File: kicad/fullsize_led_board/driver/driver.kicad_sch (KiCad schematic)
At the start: 131 parts, among them J4 Anodes Header, J5 Cathodes Header, Q1 SQ2351CES, Q10 SQ2351CES, Q11 SQ2351CES, Q12 SQ2351CES, Q13 SQ2351CES, Q14 SQ2351CES, Q15 SQ2351CES, Q16 SQ2351CES, Q17 SQ2351CES, Q18 SQ2351CES, Q19 SQ2351CES, Q2 SQ2351CES, Q20 SQ2351CES, Q21 SQ2351CES, Q22 SQ2351CES, Q23 SQ2351CES, Q24 SQ2351CES, Q3 SQ2351CES, Q4 SQ2351CES, Q5 SQ2351CES, Q6 SQ2351CES, Q7 SQ2351CES, Q8 SQ2351CES, Q9 SQ2351CES, U1 74HCT541, U2 74HCT595, U3 74HCT595, U4 74HCT595, U5 TPIC6B595N, U6 TPIC6B595N, U7 TPIC6B595N, U8 TPIC6B595N

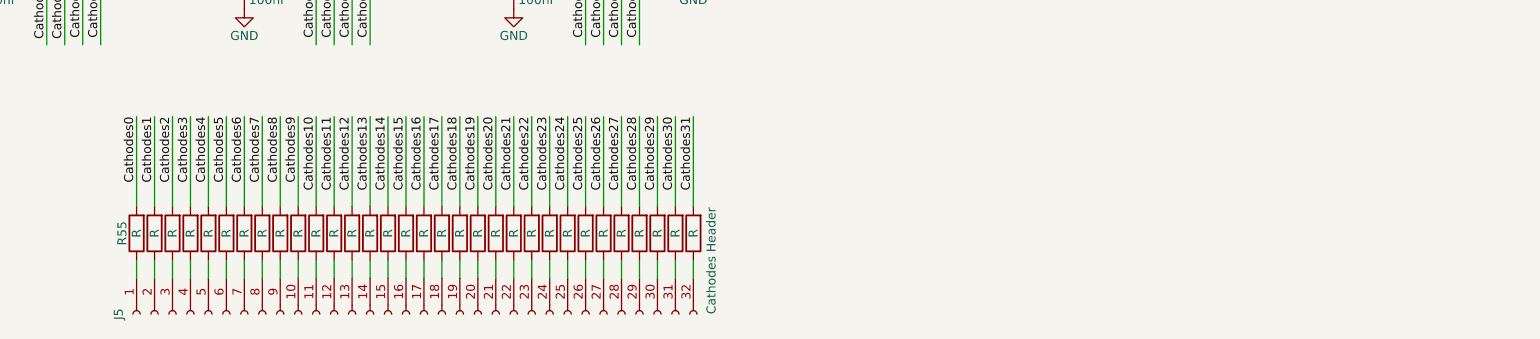
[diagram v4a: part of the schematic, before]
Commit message: kicad: finalized led resistor values
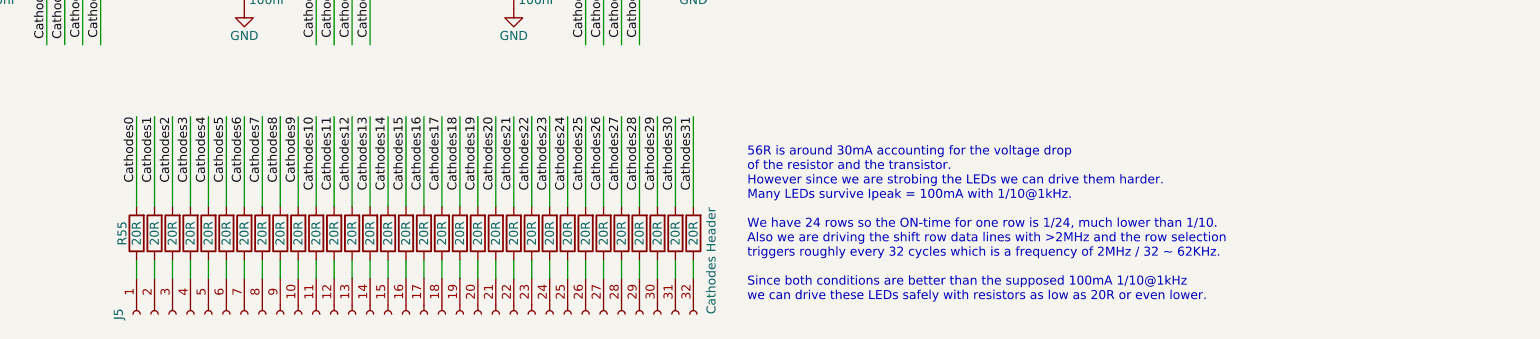
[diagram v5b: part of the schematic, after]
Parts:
- R55, R56, R57, R58, R59, R60, R61, R62, R63, R64, R65, R66, R67, R68, R69, R70, R71, R72, R73, R74, R75, R76, R77, R78, R79, R80, R81, R82, R83, R84, R85, R86: value R -> 20R
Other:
- note added: "56R is around 30mA accounting for the voltage drop of the resistor and the transistor. However since we are strobing the LEDs we can drive them harder. Many LEDs survive Ipeak = 100mA with 1/10@1kHz. We have 24 rows so the ON-time for one row is 1/24, much lower than 1/10. Also we are driving the shift row data lines with >2MHz and the row selection triggers roughly every 32 cycles which is a fre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"
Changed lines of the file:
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@@
 		)
 	)
+	(text "56R is around 30mA accounting for the voltage drop\nof the resistor and the transistor.\nHowever since we are strobing the LEDs we can drive them harder.\nMany LEDs survive Ipeak = 100mA with 1/10@1kHz.\n\nWe have 24 rows so the ON-time for one row is 1/24, much lower than 1/10.\nAlso we are driving the shift row data lines with >2MHz and the row selection\ntriggers roughly every 32 cycles which is a frequency of 2MHz / 32 ~ 62KHz.\n\nSince both conditions are better than the supposed 100mA 1/10@1kHz\nwe can drive these LEDs safely with resistors as low as 20R or even lower."
+		(exclude_from_sim no)
+		(at 203.2 266.7 0)
+		(effects
+			(font
+				(size 1.27 1.27)
+			)
+			(justify left)
+		)
+	)
 	(text "Pin GND refers to FPGA GND."
 		(exclude_from_sim no)
@@
 			)
 		)
-		(property "Value" "R"
+		(property "Value" "20R"
 			(at 175.26 267.97 90)
 			(effects
@@
 			)
 		)
-		(property "Value" "R"
+		(property "Value" "20R"
 			(at 193.04 267.97 90)
 			(effects
@@
 			)
 		)
-		(property "Value" "R"
+		(property "Value" "20R"
 			(at 137.16 267.97 90)
 			(effects
@@
 			)
 		)
-		(property "Value" "R"
+		(property "Value" "20R"
 			(at 162.56 267.97 90)
 			(effects
@@
 			)
 		)
-		(property "Value" "R"
+		(property "Value" "20R"
 			(at 132.08 267.97 90)
 			(effects
@@
 			)
 		)
-		(property "Value" "R"
+		(property "Value" "20R"
 			(at 127 267.97 90)
 			(effects
@@
 			)
 		)
-		(property "Value" "R"
+		(property "Value" "20R"
 			(at 116.84 267.97 90)
 			(effects
@@
 			)
 		)
-		(property "Value" "R"
+		(property "Value" "20R"
 			(at 187.96 267.97 90)
 			(effects
@@
 			)
 		)
-		(property "Value" "R"
+		(property "Value" "20R"
 			(at 177.8 267.97 90)
 			(effects
@@
 			)
 		)
-		(property "Value" "R"
+		(property "Value" "20R"
 			(at 144.78 267.97 90)
 			(effects
@@
 			)
 		)
-		(property "Value" "R"
+		(property "Value" "20R"
 			(at 157.48 267.97 90)
 			(effects
@@
 			)
 		)
-		(property "Value" "R"
+		(property "Value" "20R"
 			(at 134.62 267.97 90)
 			(effects
@@
 			)
 		)
-		(property "Value" "R"
+		(property "Value" "20R"
 			(at 119.38 267.97 90)
 			(effects
@@
 			)
 		)
-		(property "Value" "R"
+		(property "Value" "20R"
 			(at 180.34 267.97 90)
 			(effects
@@
 			)
 		)
-		(property "Value" "R"
+		(property "Value" "20R"
 			(at 149.86 267.97 90)
 			(effects
@@
 			)
 		)
-		(property "Value" "R"
+		(property "Value" "20R"
 			(at 160.02 267.97 90)
 			(effects
@@
 			)
 		)
-		(property "Value" "R"
+		(property "Value" "20R"
 			(at 139.7 267.97 90)
 			(effects
@@
 			)
 		)
-		(property "Value" "R"
+		(property "Value" "20R"
 			(at 124.46 267.97 90)
 			(effects
@@
 			)
 		)
-		(property "Value" "R"
+		(property "Value" "20R"
 			(at 154.94 267.97 90)
 			(effects
@@
 			)
 		)
-		(property "Value" "R"
+		(property "Value" "20R"
 			(at 182.88 267.97 90)
 			(effects
@@
 			)
 		)
-		(property "Value" "R"
+		(property "Value" "20R"
 			(at 190.5 267.97 90)
 			(effects
@@
 			)
 		)
-		(property "Value" "R"
+		(property "Value" "20R"
 			(at 152.4 267.97 90)
 			(effects
@@
 			)
 		)
-		(property "Value" "R"
+		(property "Value" "20R"
 			(at 172.72 267.97 90)
 			(effects
@@
 			)
 		)
-		(property "Value" "R"
+		(property "Value" "20R"
 			(at 121.92 267.97 90)
 			(effects
@@
 			)
 		)
-		(property "Value" "R"
+		(property "Value" "20R"
 			(at 185.42 267.97 90)
 			(effects
@@
 			)
 		)
-		(property "Value" "R"
+		(property "Value" "20R"
 			(at 142.24 267.97 90)
 			(effects
@@
 			)
 		)
-		(property "Value" "R"
+		(property "Value" "20R"
 			(at 129.54 267.97 90)
 			(effects
@@
 			)
 		)
-		(property "Value" "R"
+		(property "Value" "20R"
 			(at 195.58 267.97 90)
 			(effects
@@
 			)
 		)
-		(property "Value" "R"
+		(property "Value" "20R"
 			(at 170.18 267.97 90)
 			(effects
@@
 			)
 		)
-		(property "Value" "R"
+		(property "Value" "20R"
 			(at 167.64 267.97 90)
 			(effects
@@
 			)
 		)
-		(property "Value" "R"
+		(property "Value" "20R"
 			(at 147.32 267.97 90)
 			(effects
@@
 			)
 		)
-		(property "Value" "R"
+		(property "Value" "20R"
 			(at 165.1 267.97 90)
 			(effects

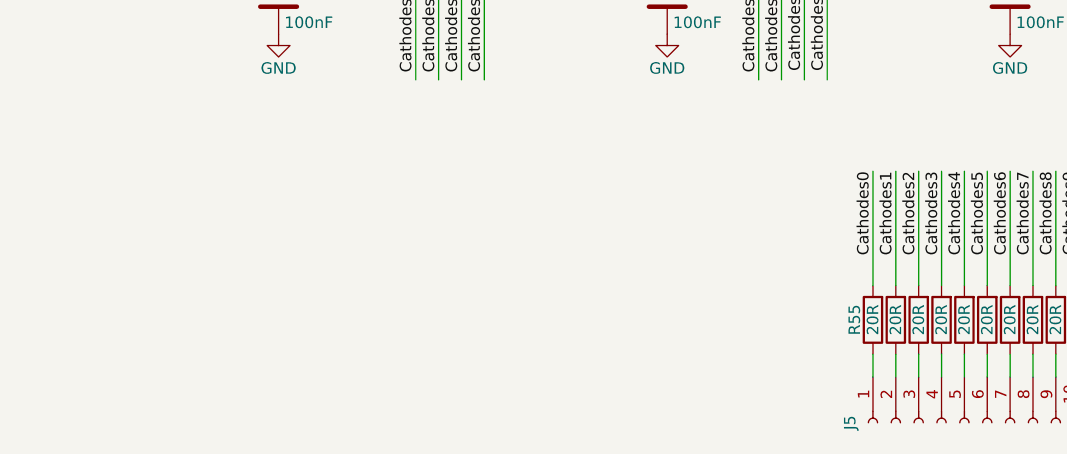
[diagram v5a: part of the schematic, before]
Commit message: misc: it works but oops, i messed up the driver's pcb layout
See notes.md on how and why.
The new version of the board will have the row data shift registers wired up correctly.
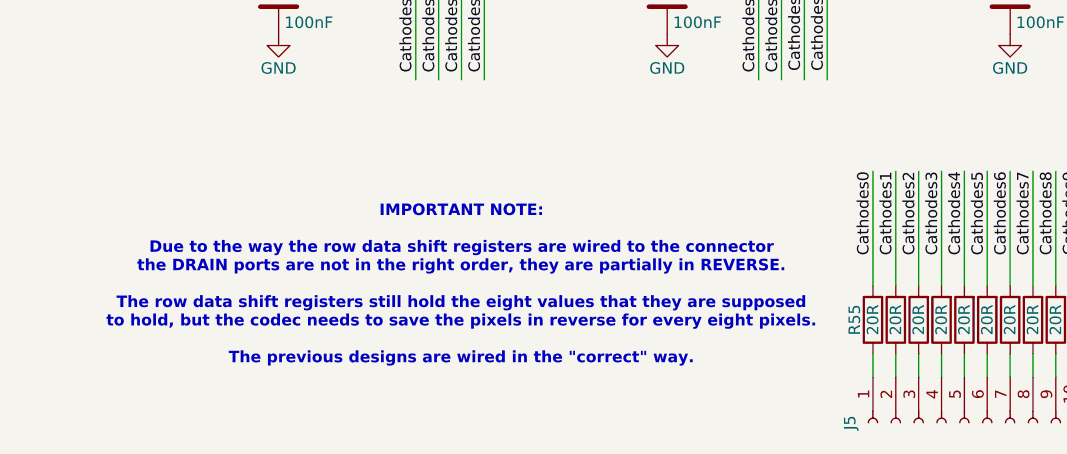
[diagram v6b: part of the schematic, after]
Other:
- note added: "IMPORTANT NOTE: Due to the way the row data shift registers are wired to the connector the DRAIN ports are not in the right order, they are partially in REVERSE. The row data shift registers still hold the eight values that they are supposed to hold, but the codec needs to save the pixels in reverse for every eight pixels. The previous designs are wired in the "correct" way."
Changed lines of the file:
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@@
+		)
+	)
+	(text "IMPORTANT NOTE:\n\nDue to the way the row data shift registers are wired to the connector\nthe DRAIN ports are not in the right order, they are partially in REVERSE.\n\nThe row data shift registers still hold the eight values that they are supposed\nto hold, but the codec needs to save the pixels in reverse for every eight pixels.\n\nThe previous designs are wired in the \"correct\" way."
+		(exclude_from_sim no)
+		(at 71.12 264.16 0)
+		(effects
+			(font
+				(size 1.27 1.27)
+				(thickness 0.254)
+				(bold yes)
+				(color 255 0 0 1)
+			)
 		)
 	)

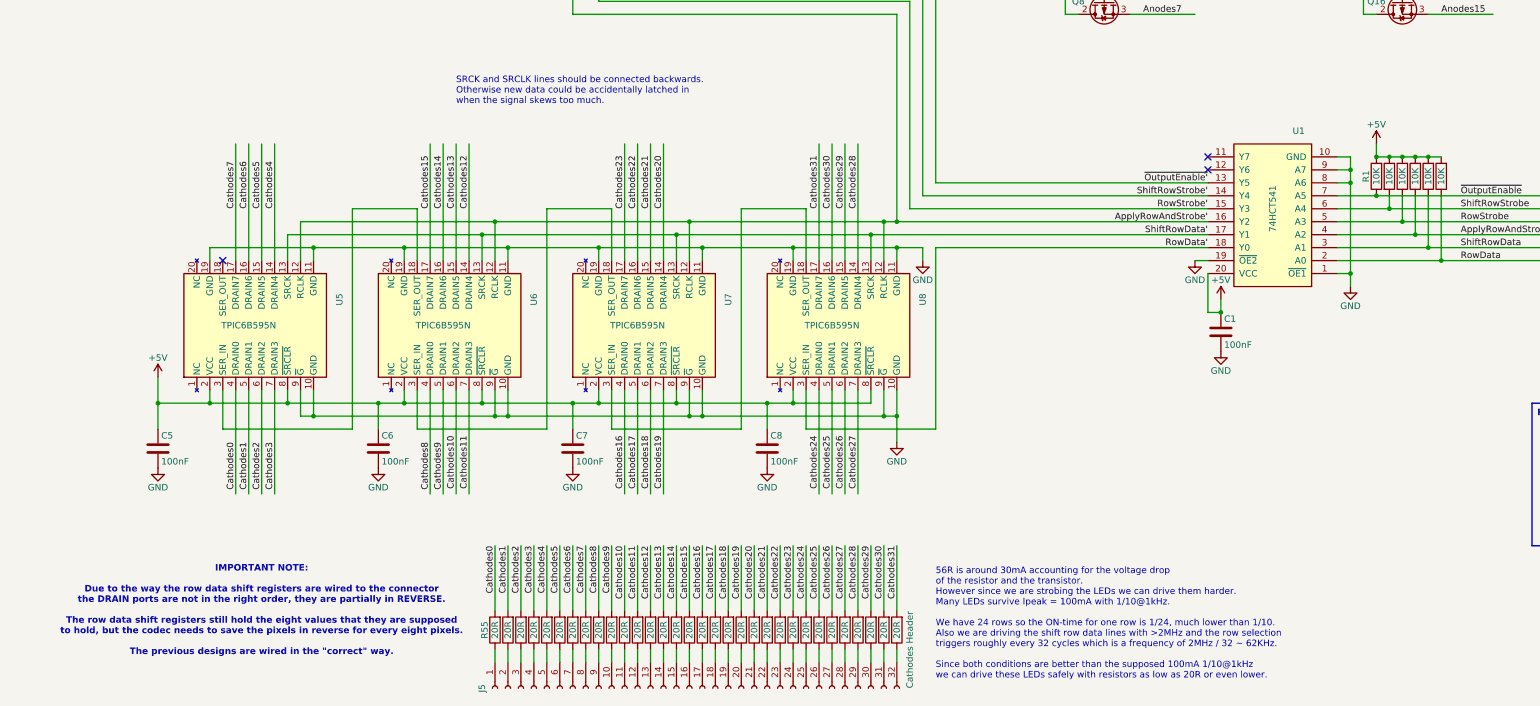
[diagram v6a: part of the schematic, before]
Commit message: fullsize led board: fixed backwards wiring
It's not as beautiful as I'd like to have it, but this will suffice, otherwise it will take way too much time to reroute the VIAs.
If I want to improve this design further, I'd like to use SMD resistors anyway, so a full rerout would be necessary.
Lesson learned I guess...
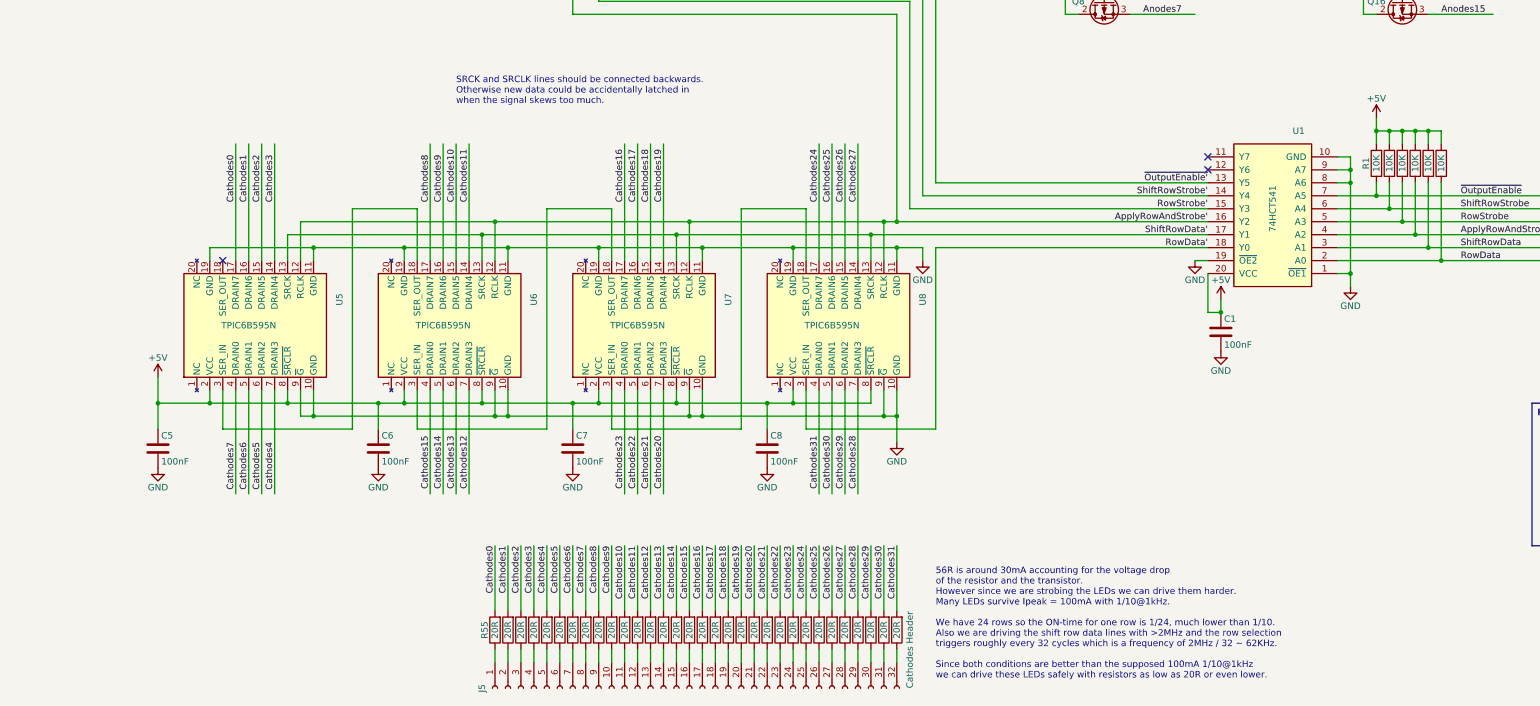
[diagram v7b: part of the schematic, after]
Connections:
- net +5V: now also R2.2; no longer R2.1
- net Cathodes0: now also U5.17 (DRAIN7); no longer U5.4 (DRAIN0)
- net Cathodes1: now also U5.16 (DRAIN6); no longer U5.5 (DRAIN1)
- net Cathodes10: now also U6.15 (DRAIN5); no longer U6.6 (DRAIN2)
- net Cathodes11: now also U6.14 (DRAIN4); no longer U6.7 (DRAIN3)
- net Cathodes12: now also U6.7 (DRAIN3); no longer U6.14 (DRAIN4)
- net Cathodes13: now also U6.6 (DRAIN2); no longer U6.15 (DRAIN5)
- net Cathodes14: now also U6.5 (DRAIN1); no longer U6.16 (DRAIN6)
- net Cathodes15: now also U6.4 (DRAIN0); no longer U6.17 (DRAIN7)
- net Cathodes16: now also U7.17 (DRAIN7); no longer U7.4 (DRAIN0)
- net Cathodes17: now also U7.16 (DRAIN6); no longer U7.5 (DRAIN1)
- net Cathodes18: now also U7.15 (DRAIN5); no longer U7.6 (DRAIN2)
- net Cathodes19: now also U7.14 (DRAIN4); no longer U7.7 (DRAIN3)
- net Cathodes2: now also U5.15 (DRAIN5); no longer U5.6 (DRAIN2)
- net Cathodes20: now also U7.7 (DRAIN3); no longer U7.14 (DRAIN4)
- net Cathodes21: now also U7.6 (DRAIN2); no longer U7.15 (DRAIN5)
- net Cathodes22: now also U7.5 (DRAIN1); no longer U7.16 (DRAIN6)
- net Cathodes23: now also U7.4 (DRAIN0); no longer U7.17 (DRAIN7)
- net Cathodes24: now also U8.17 (DRAIN7); no longer U8.4 (DRAIN0)
- net Cathodes25: now also U8.16 (DRAIN6); no longer U8.5 (DRAIN1)
- net Cathodes26: now also U8.15 (DRAIN5); no longer U8.6 (DRAIN2)
- net Cathodes27: now also U8.14 (DRAIN4); no longer U8.7 (DRAIN3)
- net Cathodes28: now also U8.7 (DRAIN3); no longer U8.14 (DRAIN4)
- net Cathodes29: now also U8.6 (DRAIN2); no longer U8.15 (DRAIN5)
- net Cathodes3: now also U5.14 (DRAIN4); no longer U5.7 (DRAIN3)
- net Cathodes30: now also U8.5 (DRAIN1); no longer U8.16 (DRAIN6)
- net Cathodes31: now also U8.4 (DRAIN0); no longer U8.17 (DRAIN7)
- net Cathodes4: now also U5.7 (DRAIN3); no longer U5.14 (DRAIN4)
- net Cathodes5: now also U5.6 (DRAIN2); no longer U5.15 (DRAIN5)
- net Cathodes6: now also U5.5 (DRAIN1); no longer U5.16 (DRAIN6)
- net Cathodes7: now also U5.4 (DRAIN0); no longer U5.17 (DRAIN7)
- net Cathodes8: now also U6.17 (DRAIN7); no longer U6.4 (DRAIN0)
- net Cathodes9: now also U6.16 (DRAIN6); no longer U6.5 (DRAIN1)
- net ShiftRowStrobe: now also R2.1; no longer R2.2
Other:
- note removed: "IMPORTANT NOTE: Due to the way the row data shift registers are wired to the connector the DRAIN ports are not in the right order, they are partially in REVERSE. The row data shift registers still hold the eight values that they are supposed to hold, but the codec needs to save the pixels in reverse for every eight pixels. The previous designs are wired in the "correct" way."
- moved on the sheet: R1
